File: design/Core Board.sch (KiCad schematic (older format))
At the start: 25 parts, among them P1 BDM, P2 jumper, SW1 SW_PUSH, U2 MC9S12XDP512, X1 CRYSTAL

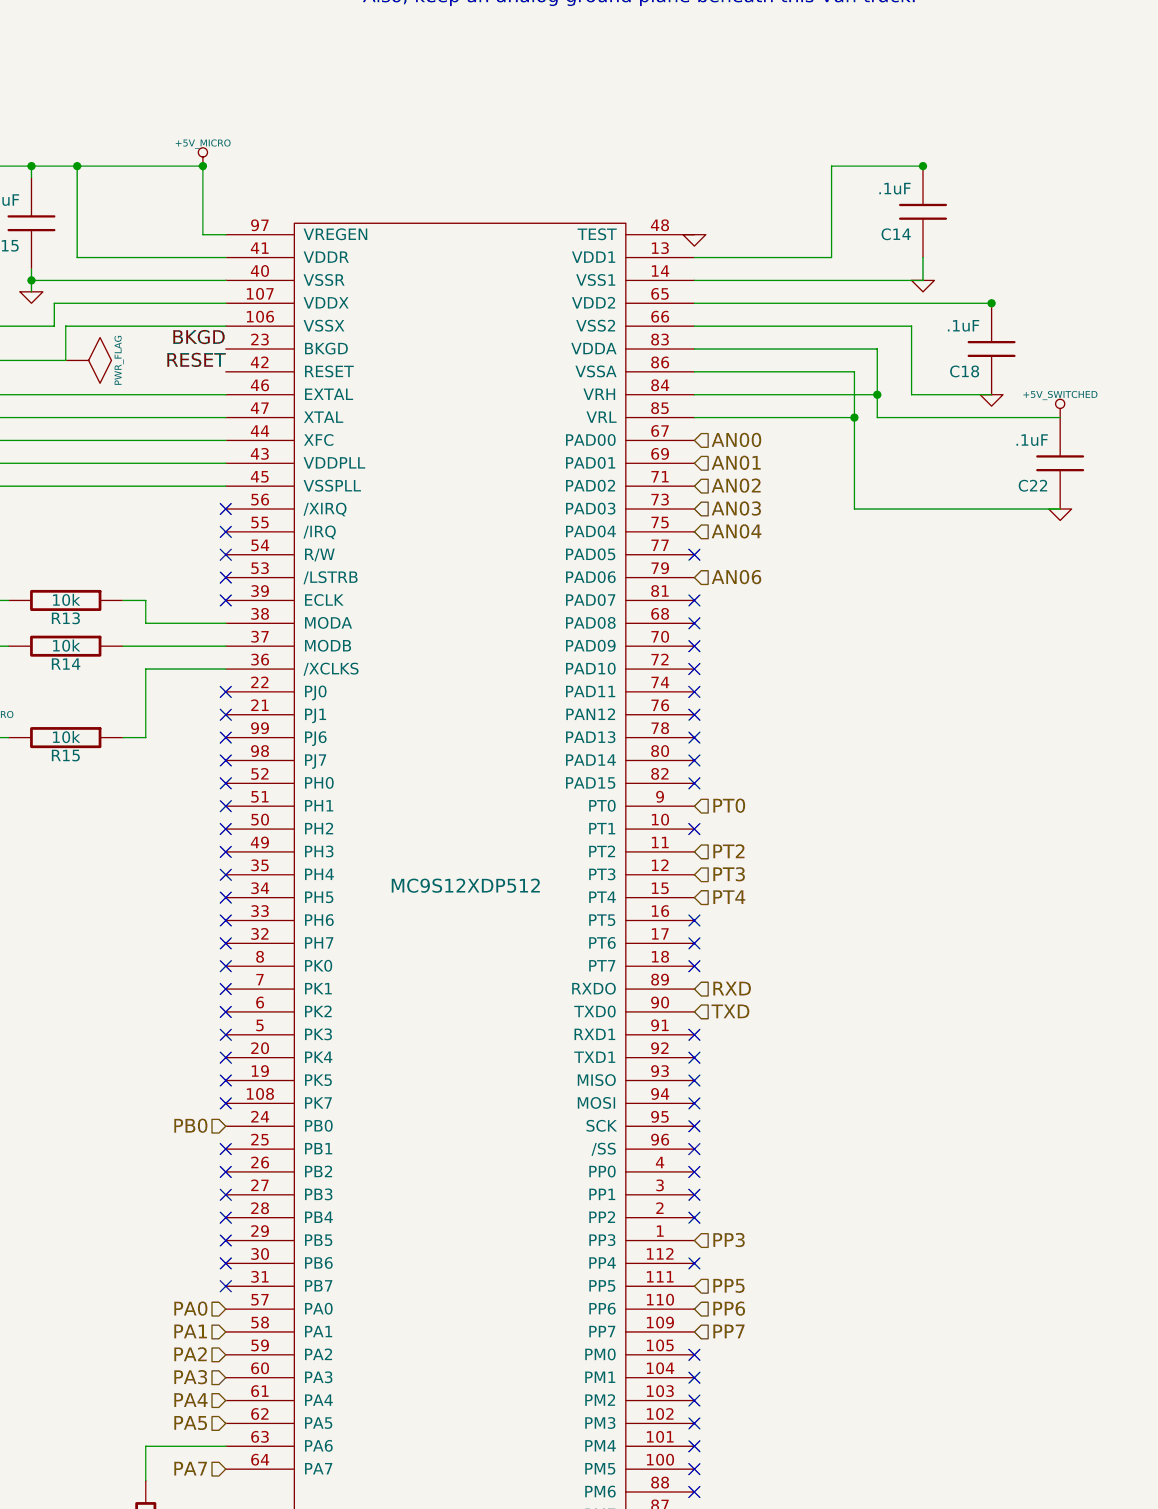
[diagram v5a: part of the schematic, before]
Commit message: use max9924 to replace ncv1124, add narrow band oxygen sensor differential input circuit, put all component into PCB edge
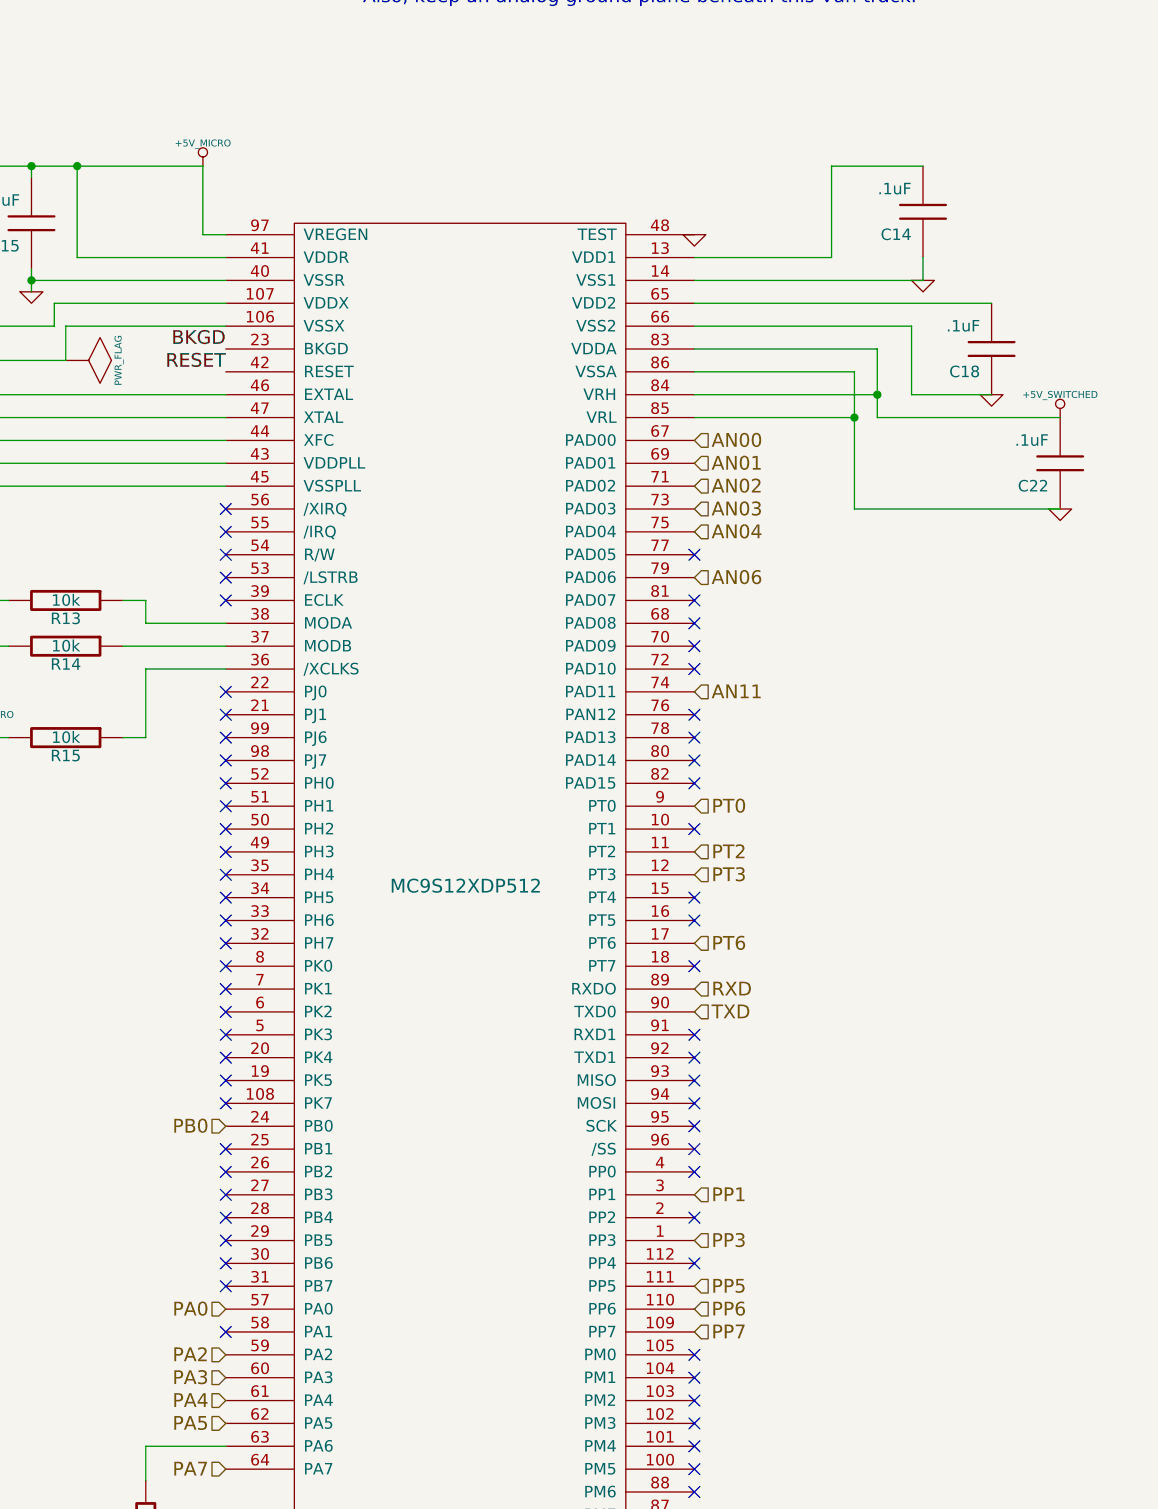
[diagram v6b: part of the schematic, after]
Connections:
- net PT6: now reaches U2.17 (PT6)
- net PP1: now reaches U2.3 (PP1)
- net AN11: now reaches U2.74 (PAD11)
- net PA1: no longer names the net of U2.58 (PA1)
- net PT4: no longer names the net of U2.15 (PT4)
- no-connect marks 65 -> 64
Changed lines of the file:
@@
-EESchema Schematic File Version 2  date 14/01/2012 13:46:11
+EESchema Schematic File Version 2  date 21/01/2012 01:12:26
 LIBS:power
 LIBS:device
@@
 LIBS:contrib
 LIBS:valves
+LIBS:freeEMS_lib
 LIBS:mainboard-cache
 EELAYER 25  0
 EELAYER END
 $Descr A3 16535 11700
-Sheet 3 12
+Sheet 5 12
 Title "CPU circuit"
-Date "14 jan 2012"
+Date "20 jan 2012"
 Rev "0.01"
 Comp "diyefi.org"
@@
 Comment4 ""
 $EndDescr
+Text HLabel 10650 5150 2    60   Input ~ 0
+AN11
+NoConn ~ 8600 7950
+NoConn ~ 10650 6050
 $Comp
 L PWR_FLAG #FLG1
@@
 $EndComp
 $Comp
-L +5V_SWITCHED #PWR26
+L +5V_SWITCHED #PWR56
 U 1 1 4EFBB324
 P 12250 3950
-F 0 "#PWR26" H 12250 3900 20  0001 C CNN
+F 0 "#PWR56" H 12250 3900 20  0001 C CNN
 F 1 "+5V_SWITCHED" H 12250 4050 30  0000 C CNN
 	1    12250 3950
@@
 $EndComp
 NoConn ~ 10650 4550
-Connection ~ 8500 2850
-$Comp
-L +5V_MICRO #PWR31
+$Comp
+L +5V_MICRO #PWR61
 U 1 1 4EFB34CE
 P 6200 5200
-F 0 "#PWR31" H 6200 5150 20  0001 C CNN
+F 0 "#PWR61" H 6200 5150 20  0001 C CNN
 F 1 "+5V_MICRO" H 6200 5300 30  0000 C CNN
 	1    6200 5200
@@
 $EndComp
 $Comp
-L +5V_MICRO #PWR32
+L +5V_MICRO #PWR62
 U 1 1 4EFB34CB
 P 7550 5350
-F 0 "#PWR32" H 7550 5300 20  0001 C CNN
+F 0 "#PWR62" H 7550 5300 20  0001 C CNN
 F 1 "+5V_MICRO" H 7550 5450 30  0000 C CNN
 	1    7550 5350
@@
 $EndComp
 $Comp
-L +5V_MICRO #PWR20
+L +5V_MICRO #PWR50
 U 1 1 4EFB34C6
 P 8500 2850
-F 0 "#PWR20" H 8500 2800 20  0001 C CNN
+F 0 "#PWR50" H 8500 2800 20  0001 C CNN
 F 1 "+5V_MICRO" H 8500 2950 30  0000 C CNN
 	1    8500 2850
@@
 Wire Wire Line
 	7950 2850 7950 3250
-Connection ~ 11650 2850
 Connection ~ 5400 3350
 Wire Wire Line
@@
 	5000 3350 5000 3650
 Connection ~ 5000 3350
-Connection ~ 11950 3450
 Wire Wire Line
 	7750 2900 7750 2850
@@
 	1    0    0    -1
 $EndComp
-Text HLabel 10650 6050 2    60   Input ~ 0
-PT4
-$Comp
-L GND #PWR35
+Text HLabel 10650 6250 2    60   Input ~ 0
+PT6
+$Comp
+L GND #PWR65
 U 1 1 4EF8A1A8
 P 8250 9600
-F 0 "#PWR35" H 8250 9600 30  0001 C CNN
+F 0 "#PWR65" H 8250 9600 30  0001 C CNN
 F 1 "GND" H 8250 9530 30  0001 C CNN
 	1    8250 9600
@@
 $EndComp
 NoConn ~ 10650 7250
-NoConn ~ 10650 7350
 NoConn ~ 10650 7450
 NoConn ~ 10650 7650
 NoConn ~ 10650 4750
 NoConn ~ 10650 6350
-NoConn ~ 10650 6250
 NoConn ~ 10650 6150
 NoConn ~ 10650 5750
@@
 RESET
 $Comp
-L GND #PWR34
+L GND #PWR64
 U 1 1 4EF89428
 P 4450 7850
-F 0 "#PWR34" H 4450 7850 30  0001 C CNN
+F 0 "#PWR64" H 4450 7850 30  0001 C CNN
 F 1 "GND" H 4450 7780 30  0001 C CNN
 	1    4450 7850
@@
 NoConn ~ 4650 6100
 $Comp
-L GND #PWR33
+L GND #PWR63
 U 1 1 4EF89423
 P 5550 5950
-F 0 "#PWR33" H 5550 5950 30  0001 C CNN
+F 0 "#PWR63" H 5550 5950 30  0001 C CNN
 F 1 "GND" H 5550 5880 30  0001 C CNN
 	1    5550 5950
@@
 $EndComp
 $Comp
-L GND #PWR22
+L GND #PWR52
 U 1 1 4EF89421
 P 11650 3350
-F 0 "#PWR22" H 11650 3350 30  0001 C CNN
+F 0 "#PWR52" H 11650 3350 30  0001 C CNN
 F 1 "GND" H 11650 3280 30  0001 C CNN
 	1    11650 3350
@@
 $EndComp
 $Comp
-L GND #PWR25
+L GND #PWR55
 U 1 1 4EF89420
 P 11950 3850
-F 0 "#PWR25" H 11950 3850 30  0001 C CNN
+F 0 "#PWR55" H 11950 3850 30  0001 C CNN
 F 1 "GND" H 11950 3780 30  0001 C CNN
 	1    11950 3850
@@
 $EndComp
 $Comp
-L GND #PWR29
+L GND #PWR59
 U 1 1 4EF8941F
 P 12250 4350
-F 0 "#PWR29" H 12250 4350 30  0001 C CNN
+F 0 "#PWR59" H 12250 4350 30  0001 C CNN
 F 1 "GND" H 12250 4280 30  0001 C CNN
 	1    12250 4350
@@
 $EndComp
 $Comp
-L GND #PWR23
+L GND #PWR53
 U 1 1 4EF8941E
 P 7750 3400
-F 0 "#PWR23" H 7750 3400 30  0001 C CNN
+F 0 "#PWR53" H 7750 3400 30  0001 C CNN
 F 1 "GND" H 7750 3330 30  0001 C CNN
 	1    7750 3400
@@
 $EndComp
 $Comp
-L GND #PWR24
+L GND #PWR54
 U 1 1 4EF8941D
 P 7400 3750
-F 0 "#PWR24" H 7400 3750 30  0001 C CNN
+F 0 "#PWR54" H 7400 3750 30  0001 C CNN
 F 1 "GND" H 7400 3680 30  0001 C CNN
 	1    7400 3750
@@
 $EndComp
 $Comp
-L GND #PWR21
+L GND #PWR51
 U 1 1 4EF8941A
 P 10650 3150
-F 0 "#PWR21" H 10650 3150 30  0001 C CNN
+F 0 "#PWR51" H 10650 3150 30  0001 C CNN
 F 1 "GND" H 10650 3080 30  0001 C CNN
 	1    10650 3150
@@
 $EndComp
 $Comp
-L GND #PWR30
+L GND #PWR60
 U 1 1 4EF89415
 P 7550 5000
-F 0 "#PWR30" H 7550 5000 30  0001 C CNN
+F 0 "#PWR60" H 7550 5000 30  0001 C CNN
 F 1 "GND" H 7550 4930 30  0001 C CNN
 	1    7550 5000
@@
 PLL + CLK
 $Comp
-L GND #PWR28
+L GND #PWR58
 U 1 1 4EF89410
 P 3950 4300
-F 0 "#PWR28" H 3950 4300 30  0001 C CNN
+F 0 "#PWR58" H 3950 4300 30  0001 C CNN
 F 1 "GND" H 3950 4230 30  0001 C CNN
 	1    3950 4300
@@
 $EndComp
 $Comp
-L GND #PWR27
+L GND #PWR57
 U 1 1 4EF8940F
 P 4400 4000
-F 0 "#PWR27" H 4400 4000 30  0001 C CNN
+F 0 "#PWR57" H 4400 4000 30  0001 C CNN
 F 1 "GND" H 4400 3930 30  0001 C CNN
 	1    4400 4000
@@
 NoConn ~ 10650 4950
 NoConn ~ 10650 5050
-NoConn ~ 10650 5150
 NoConn ~ 10650 5250
 NoConn ~ 10650 5350
@@
 Text HLabel 8600 8050 0    60   Input ~ 0
 PA2
-Text HLabel 8600 7950 0    60   Input ~ 0
-PA1
+Text HLabel 10650 7350 2    60   Input ~ 0
+PP1
 Text HLabel 8600 7850 0    60   Input ~ 0
 PA0

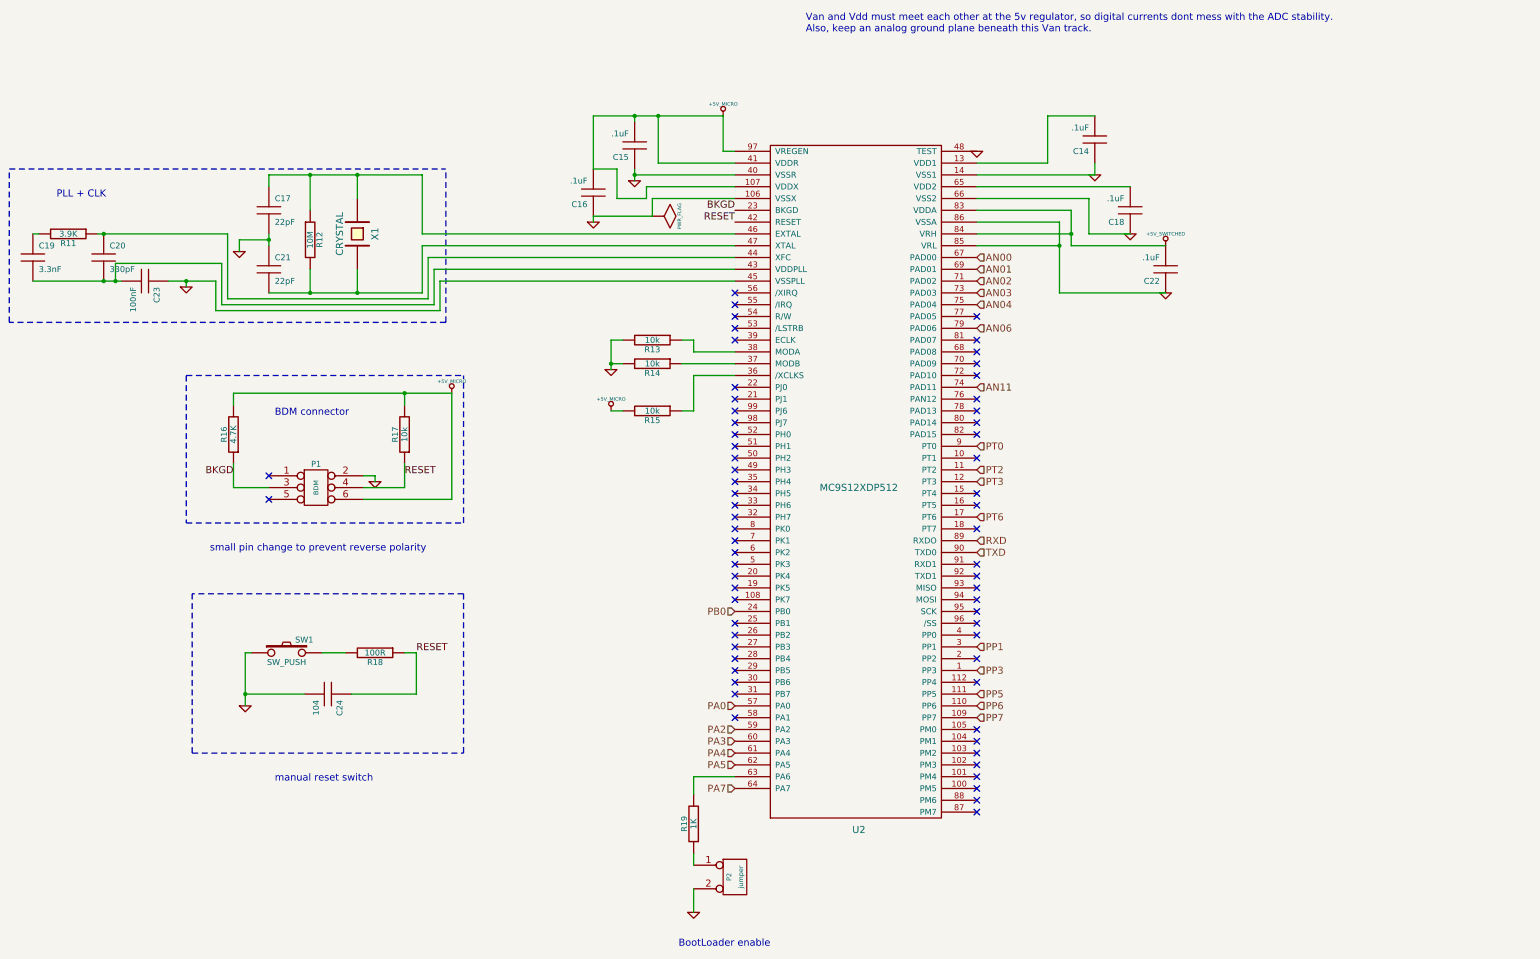
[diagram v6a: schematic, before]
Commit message: make new footprint for max9924 & lm9040, add can bus interface, generate new netlist
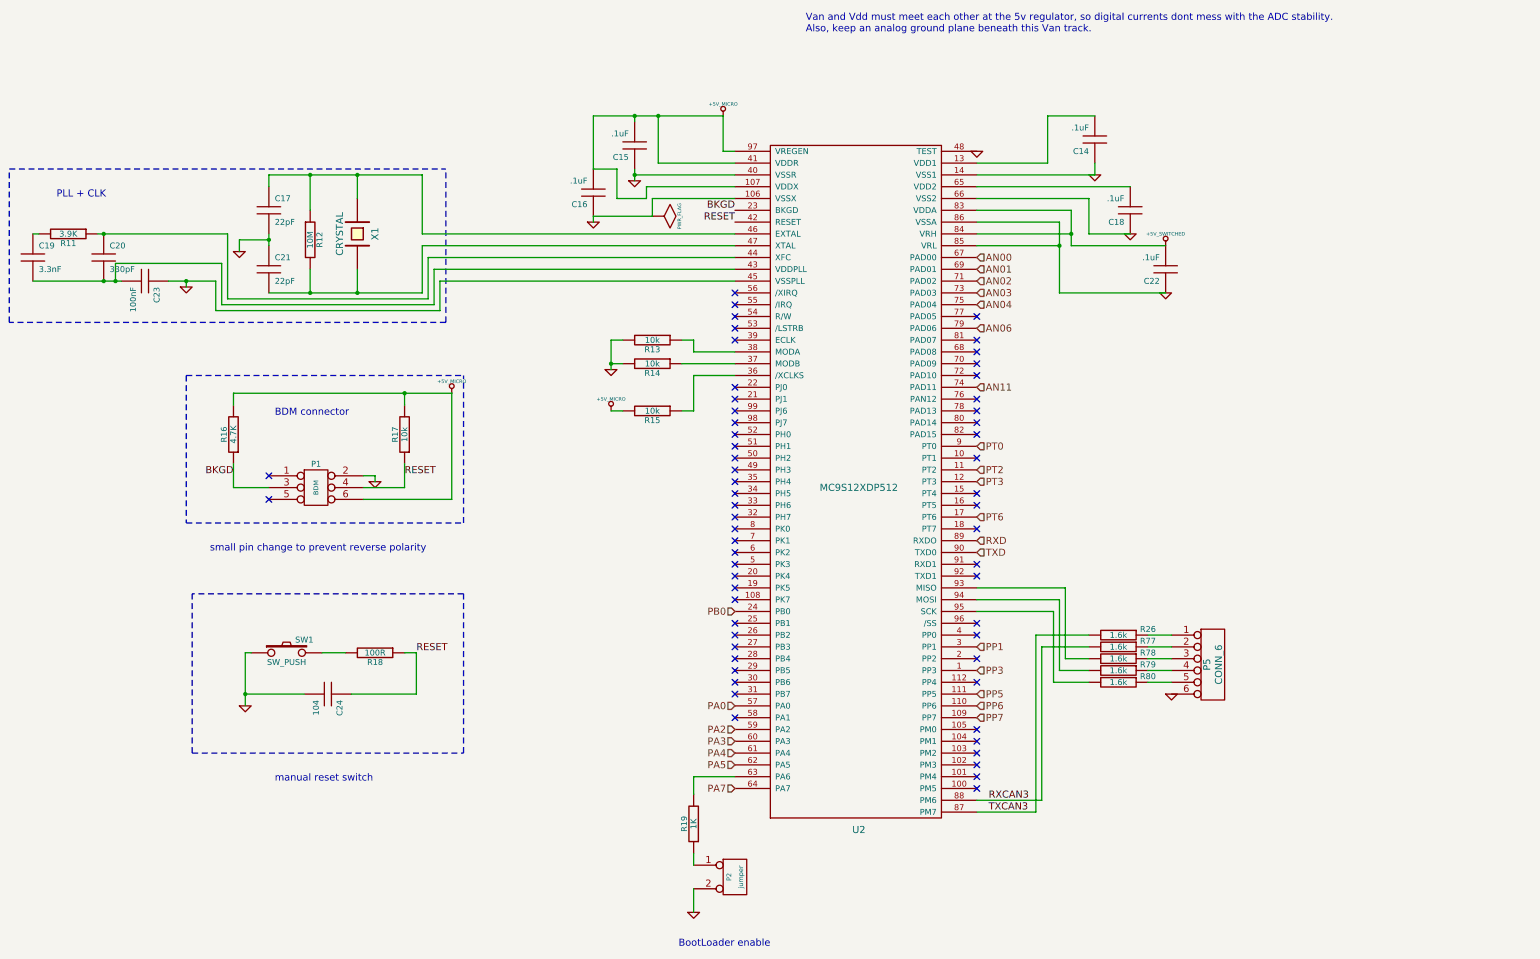
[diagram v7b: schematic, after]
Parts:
- added P5: CONN_6, symbol CONN_6
- added R26, R77, R78, R79, R80: 1.6k, symbol R
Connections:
- net GND: now also P5.6
- net TXCAN3: now reaches U2.87 (PM7)
- net TXCAN3: now also R26.2
- net RXCAN3: now reaches U2.88 (PM6)
- net RXCAN3: now also R77.2
- net at U2.93 (MISO): now also R78.2
- net at U2.94 (MOSI): now also R79.2
- net at U2.95 (SCK): now also R80.2
- new net: P5.1, R26.1
- new net: P5.2, R77.1
- new net: P5.3, R78.1
- new net: P5.4, R79.1
- new net: P5.5, R80.1
- no-connect marks 64 -> 59
